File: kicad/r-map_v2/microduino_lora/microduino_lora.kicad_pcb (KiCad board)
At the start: 2 copper layers, 3 parts, among them J1 Conn_Coaxial, U1 Microduino, U2 RFM95W-915S2

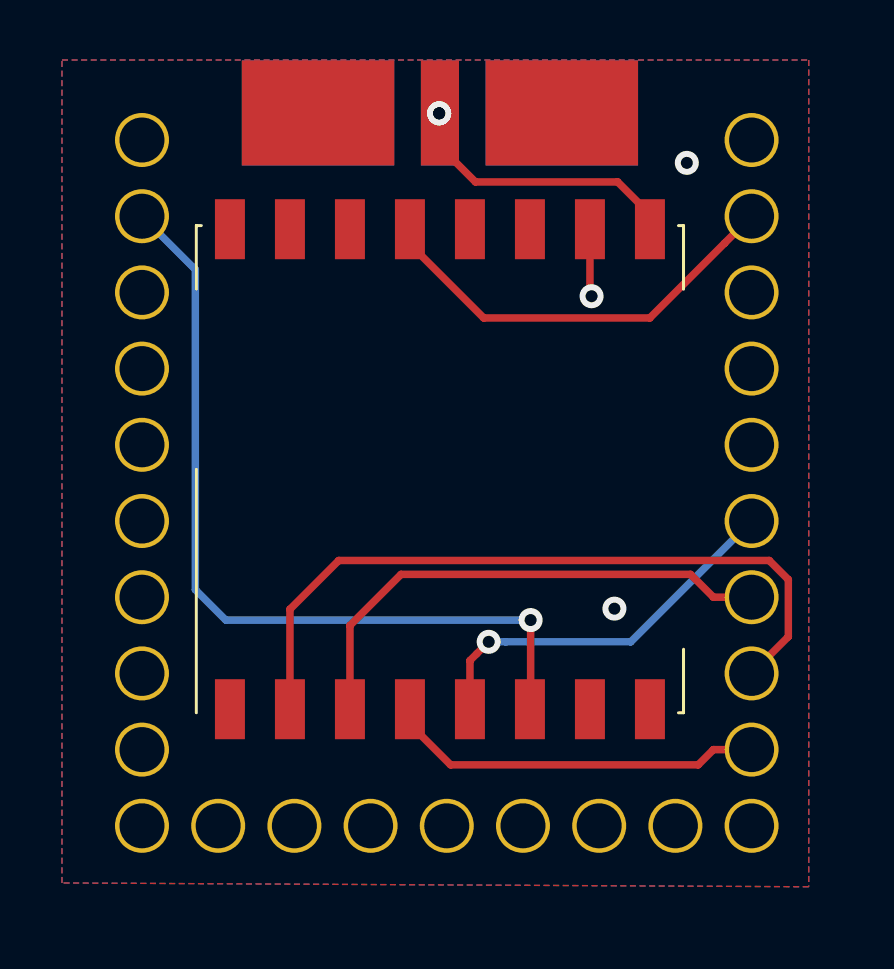
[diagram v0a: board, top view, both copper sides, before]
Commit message: Arduino lora shield Schema update e Pcb recreation
Change connection for IO pins to connect with D2 and solder pad for unused gpio pins
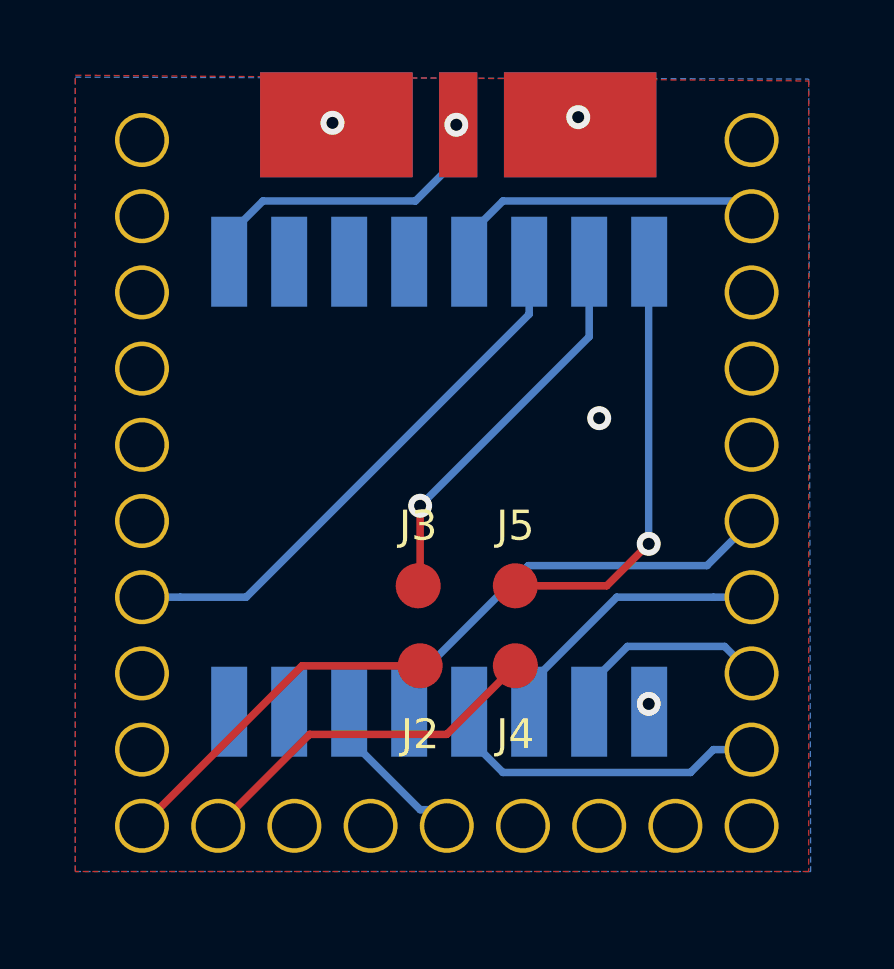
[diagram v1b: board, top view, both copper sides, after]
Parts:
- added J2: Conn_01x01, Measurement_Points:Measurement_Point_Round-SMD-Pad_Small, F.Cu at (105.4, 77.1)
- added J3: Conn_01x01, Measurement_Points:Measurement_Point_Round-SMD-Pad_Small, F.Cu at (105.3, 74.4)
- added J4: Conn_01x01, Measurement_Points:Measurement_Point_Round-SMD-Pad_Small, F.Cu at (108.6, 77.1)
- added J5: Conn_01x01, Measurement_Points:Measurement_Point_Round-SMD-Pad_Small, F.Cu at (108.6, 74.4)
- U1: footprint Rmap:microduino -> lib:microduino
- U2: value RFM95W-915S2 -> RFM95; footprint RF_Modules:Hopref_RFM9XW_SMD -> lib:RFM95; moved to B.Cu
- moved J1 0.73 mm to (106.7, 60.8)
- moved U2 0.58 mm to (106.0, 71.1)
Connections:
- U1 pad 12: Net-(U1-Pad12) -> (no net)
- U1 pad 13: Net-(U1-Pad13) -> (no net)
- U1 pad 14: Net-(U1-Pad14) -> RST
- U1 pad 15: Net-(U1-Pad15) -> (no net)
- U1 pad 16: Net-(U1-Pad16) -> (no net)
- U1 pad 17: Net-(U1-Pad17) -> (no net)
- U1 pad 18: Net-(U1-Pad18) -> (no net)
- U1 pad 2: RST -> (no net)
- U1 pad 23: Net-(U1-Pad23) -> (no net)
- U1 pad 24: Net-(U1-Pad24) -> (no net)
- U1 pad 25: Net-(U1-Pad25) -> (no net)
- U1 pad 27: Net-(U1-Pad27) -> (no net)
- U1 pad 3: Net-(U1-Pad3) -> (no net)
- U1 pad 4: Net-(U1-Pad4) -> (no net)
- U1 pad 5: Net-(U1-Pad5) -> (no net)
- U1 pad 6: Net-(U1-Pad6) -> (no net)
- U1 pad 7: Net-(U1-Pad7) -> TxRxDONE
- U1 pad 8: Net-(U1-Pad8) -> (no net)
- U1 pad 9: Net-(U1-Pad9) -> (no net)
- U2 pad 11: Net-(U2-Pad11) -> (no net)
- U2 pad 12: Net-(U2-Pad12) -> (no net)
- U2 pad 14: Net-(U2-Pad14) -> TxRxDONE
- U2 pad 15: Net-(U2-Pad15) -> RxTimeOut
- U2 pad 16: Net-(U2-Pad16) -> FSKTimeOut
- U2 pad 7: Net-(U2-Pad7) -> (no net)
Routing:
- net RST: track 27.8 -> 5.36 mm, vias 1 -> 0
- net TxRxDONE: track 0.00 -> 18.6 mm
- net MISO: track 24.5 -> 7.22 mm
- net FSKTimeOut: track 0.00 -> 14.4 mm, vias 0 -> 1
- net RxTimeOut: track 0.00 -> 13.0 mm, vias 0 -> 1
- net Net-(J4-Pad1): track 0.00 -> 12.1 mm
- net Net-(J2-Pad1): track 0.00 -> 11.5 mm
- net MOSI: track 17.2 -> 9.52 mm
- net +3V3: track 14.3 -> 11.0 mm
- net GND: track 2.26 -> 0.00 mm, vias 3 -> 4
- net NSS: track 12.9 -> 14.6 mm, vias 1 -> 0
- net SCK: track 12.7 -> 11.1 mm
- net Net-(J1-Pad1): track 9.55 -> 10.7 mm, vias 2 -> 1

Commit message: Moved via too next to net
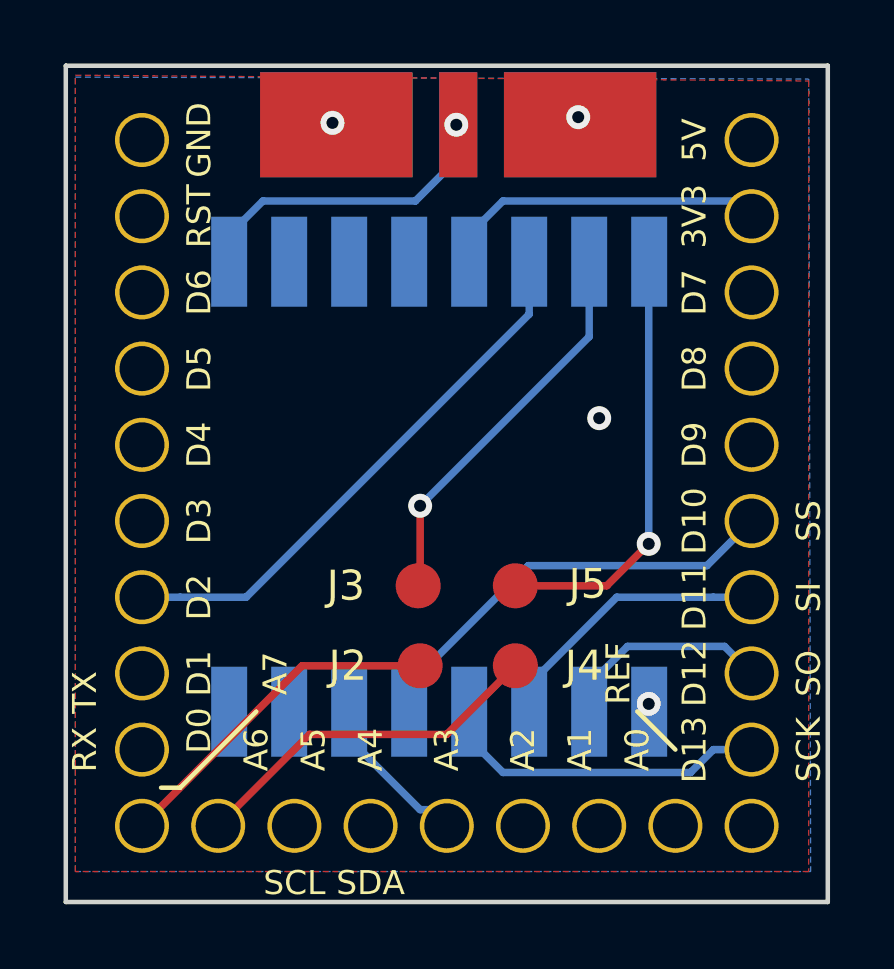
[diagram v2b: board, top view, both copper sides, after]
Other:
- board outline added: 25.4 x 27.9 mm
